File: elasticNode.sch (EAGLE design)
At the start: 101 parts, among them J1 ISP_CONN_6PIN, J2 FEMALE_HEADER_2X2, J3 FEMALE_HEADER_2X1, J4 FEMALE_HEADER_2X1, J5 FEMALE_HEADER_5X2, J6 FEMALE_HEADER_5X2, J7 JTAG_CONN_6PINTHT, J8 USB_CONN, U1 ATMEGA64AQFN, U10 LTC3419DFN, U2 SST26VF032B, U3 MRF24J40MA, U4 SPARTAN6-LX9, U5 SST26VF032B, U6 PAC1720, U7 PAC1720, U8 PAC1720, U9 FT232R, X1 12MHz, X2 50MHz, X3 32MHz

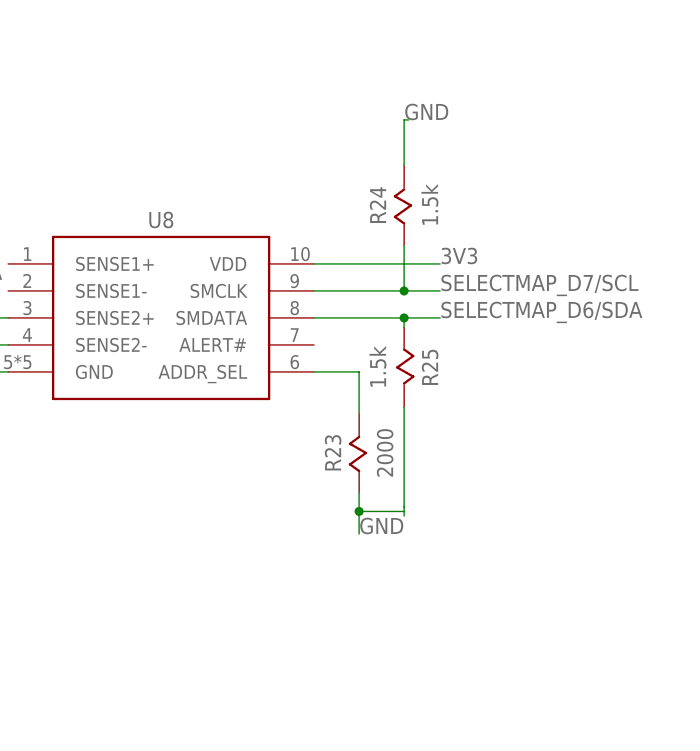
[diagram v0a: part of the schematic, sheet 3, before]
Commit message: changed i2c to pullup
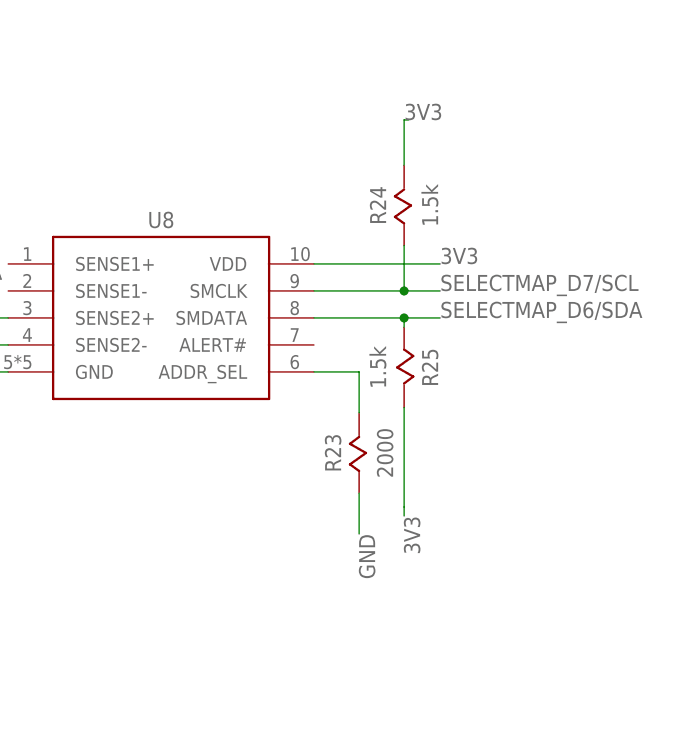
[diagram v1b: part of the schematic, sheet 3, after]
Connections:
- removed net N$33: R25.2
- net 3V3: now also R24.2, R25.2
- net GND: no longer R24.2
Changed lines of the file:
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@@
 <segment>
 <pinref part="R23" gate="G$1" pin="1"/>
-<wire x1="122" y1="-20.46" x2="122" y2="-22.5" width="0.1524" layer="91"/>
-<label x="122" y="-25" size="1.778" layer="95"/>
-<wire x1="122" y1="-22.5" x2="122" y2="-25" width="0.1524" layer="91"/>
-<wire x1="127" y1="-22.5" x2="122" y2="-22.5" width="0.1524" layer="91"/>
-<junction x="122" y="-22.5"/>
+<label x="122" y="-25" size="1.778" layer="95" rot="R270"/>
+<wire x1="122" y1="-20.46" x2="122" y2="-25" width="0.1524" layer="91"/>
 </segment>
 <segment>
@@
 <wire x1="70" y1="-7" x2="83" y2="-7" width="0.1524" layer="91"/>
 <label x="70" y="-7" size="1.778" layer="95" rot="R180"/>
-</segment>
-<segment>
-<pinref part="R24" gate="G$1" pin="2"/>
-<wire x1="127" y1="15.96" x2="127" y2="21" width="0.1524" layer="91"/>
-<wire x1="127" y1="21" x2="127.5" y2="21" width="0.1524" layer="91"/>
-<label x="127" y="21" size="1.778" layer="95"/>
 </segment>
 <segment>
@@
 <wire x1="-39" y1="8" x2="-39" y2="6.46" width="0.1524" layer="91"/>
 <label x="-27" y="0" size="1.778" layer="95"/>
+</segment>
+<segment>
+<pinref part="R24" gate="G$1" pin="2"/>
+<wire x1="127" y1="15.96" x2="127" y2="21" width="0.1524" layer="91"/>
+<wire x1="127" y1="21" x2="127.5" y2="21" width="0.1524" layer="91"/>
+<label x="127" y="21" size="1.778" layer="95"/>
+</segment>
+<segment>
+<pinref part="R25" gate="G$1" pin="2"/>
+<wire x1="127" y1="-10.96" x2="127" y2="-22" width="0.1524" layer="91"/>
+<wire x1="127" y1="-23" x2="127" y2="-22" width="0.1524" layer="91"/>
+<label x="127" y="-23" size="1.778" layer="95" rot="R270"/>
 </segment>
 </net>
@@
 </segment>
 </net>
-<net name="N$33" class="0">
-<segment>
-<pinref part="R25" gate="G$1" pin="2"/>
-<wire x1="127" y1="-10.96" x2="127" y2="-22" width="0.1524" layer="91"/>
-<wire x1="127" y1="-23" x2="127" y2="-22" width="0.1524" layer="91"/>
-</segment>
-</net>

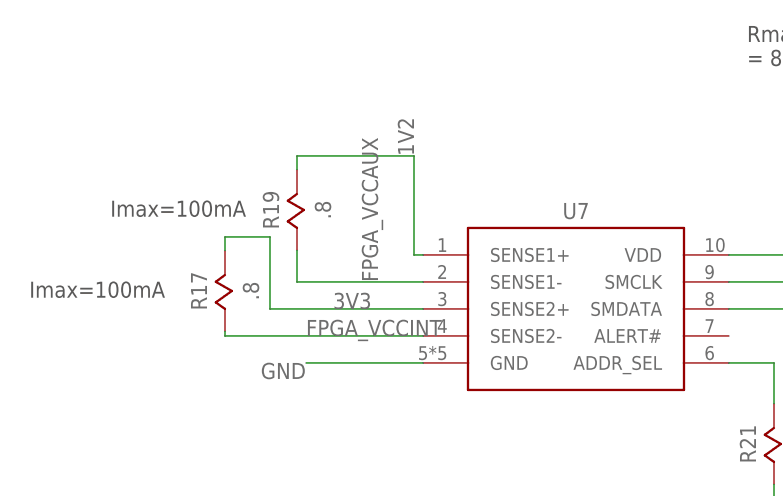
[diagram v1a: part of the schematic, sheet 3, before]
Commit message: updated board for previous pullups and swapped fpga power rails
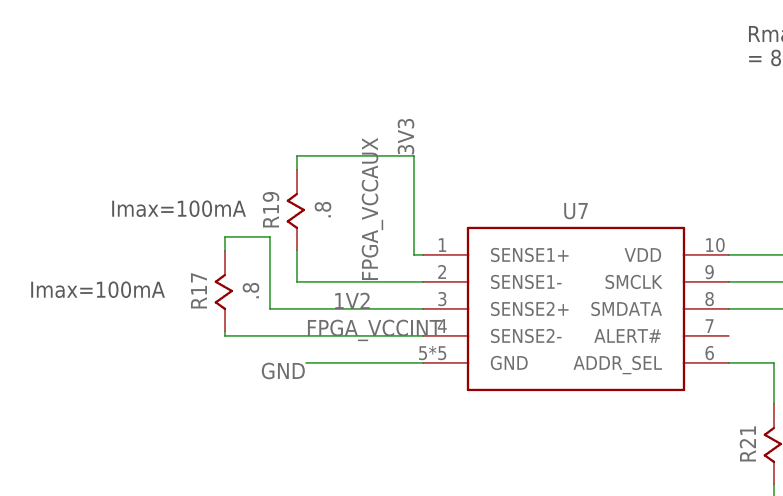
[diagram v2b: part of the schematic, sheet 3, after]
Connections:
- net 1V2: now also R17.2, U7.SENSE2+; no longer R19.2, U7.SENSE1+
- net 3V3: now also R19.2, U7.SENSE1+; no longer R17.2, U7.SENSE2+
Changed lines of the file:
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@@
-</segment>
-<segment>
-<pinref part="U7" gate="G$1" pin="SENSE2+"/>
-<wire x1="-17" y1="0" x2="-34" y2="0" width="0.1524" layer="91"/>
-<wire x1="-34" y1="0" x2="-34" y2="8" width="0.1524" layer="91"/>
-<wire x1="-34" y1="8" x2="-39" y2="8" width="0.1524" layer="91"/>
-<pinref part="R17" gate="G$1" pin="2"/>
-<wire x1="-39" y1="8" x2="-39" y2="6.46" width="0.1524" layer="91"/>
-<label x="-27" y="0" size="1.778" layer="95"/>
 </segment>
 <segment>
@@
 <wire x1="127" y1="-23" x2="127" y2="-22" width="0.1524" layer="91"/>
 <label x="127" y="-23" size="1.778" layer="95" rot="R270"/>
+</segment>
+<segment>
+<pinref part="U7" gate="G$1" pin="SENSE1+"/>
+<wire x1="-17" y1="6" x2="-18" y2="6" width="0.1524" layer="91"/>
+<wire x1="-18" y1="6" x2="-18" y2="17" width="0.1524" layer="91"/>
+<wire x1="-18" y1="17" x2="-31" y2="17" width="0.1524" layer="91"/>
+<pinref part="R19" gate="G$1" pin="2"/>
+<wire x1="-31" y1="17" x2="-31" y2="15.46" width="0.1524" layer="91"/>
+<label x="-18" y="17" size="1.778" layer="95" rot="R90"/>
 </segment>
 </net>
@@
 <net name="1V2" class="1">
 <segment>
-<pinref part="U7" gate="G$1" pin="SENSE1+"/>
-<wire x1="-17" y1="6" x2="-18" y2="6" width="0.1524" layer="91"/>
-<wire x1="-18" y1="6" x2="-18" y2="17" width="0.1524" layer="91"/>
-<wire x1="-18" y1="17" x2="-31" y2="17" width="0.1524" layer="91"/>
-<pinref part="R19" gate="G$1" pin="2"/>
-<wire x1="-31" y1="17" x2="-31" y2="15.46" width="0.1524" layer="91"/>
-<label x="-18" y="17" size="1.778" layer="95" rot="R90"/>
+<pinref part="U7" gate="G$1" pin="SENSE2+"/>
+<wire x1="-17" y1="0" x2="-34" y2="0" width="0.1524" layer="91"/>
+<wire x1="-34" y1="0" x2="-34" y2="8" width="0.1524" layer="91"/>
+<wire x1="-34" y1="8" x2="-39" y2="8" width="0.1524" layer="91"/>
+<pinref part="R17" gate="G$1" pin="2"/>
+<wire x1="-39" y1="8" x2="-39" y2="6.46" width="0.1524" layer="91"/>
+<label x="-27" y="0" size="1.778" layer="95"/>
 </segment>
 </net>

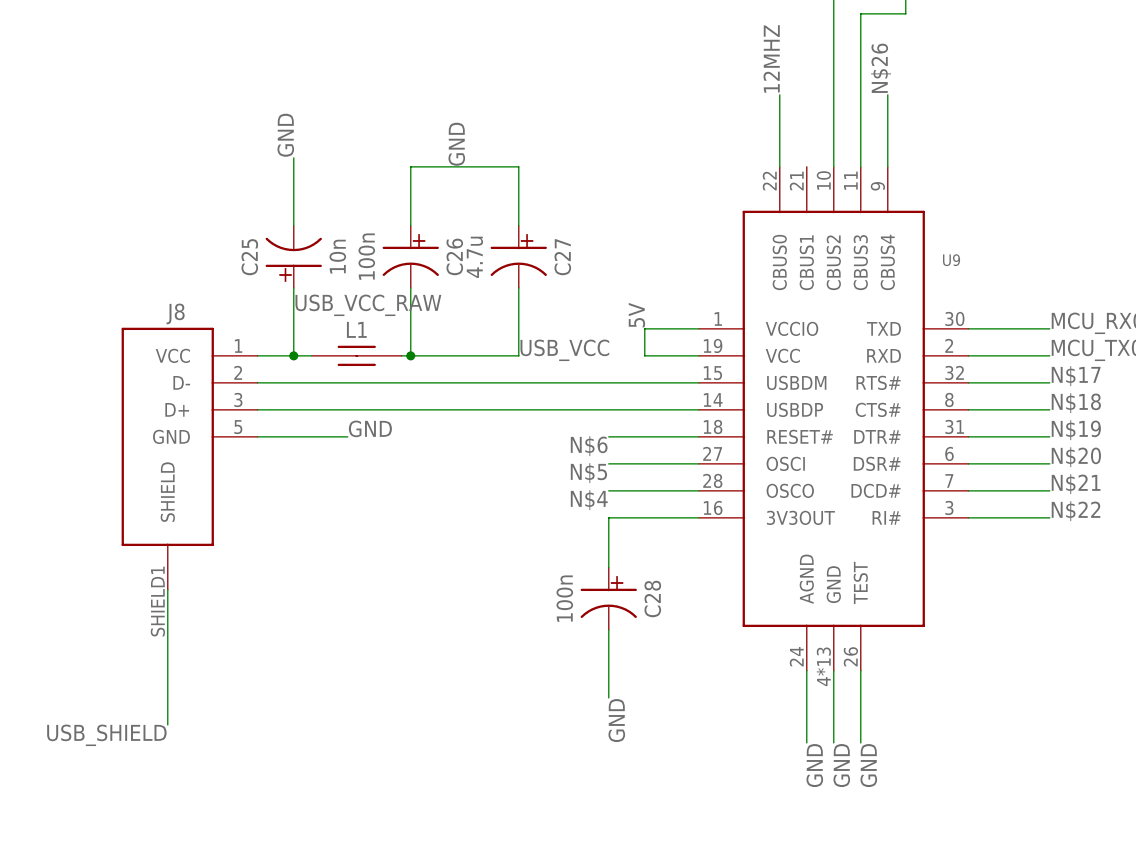
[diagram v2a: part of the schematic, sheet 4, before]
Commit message: added smd usb connector
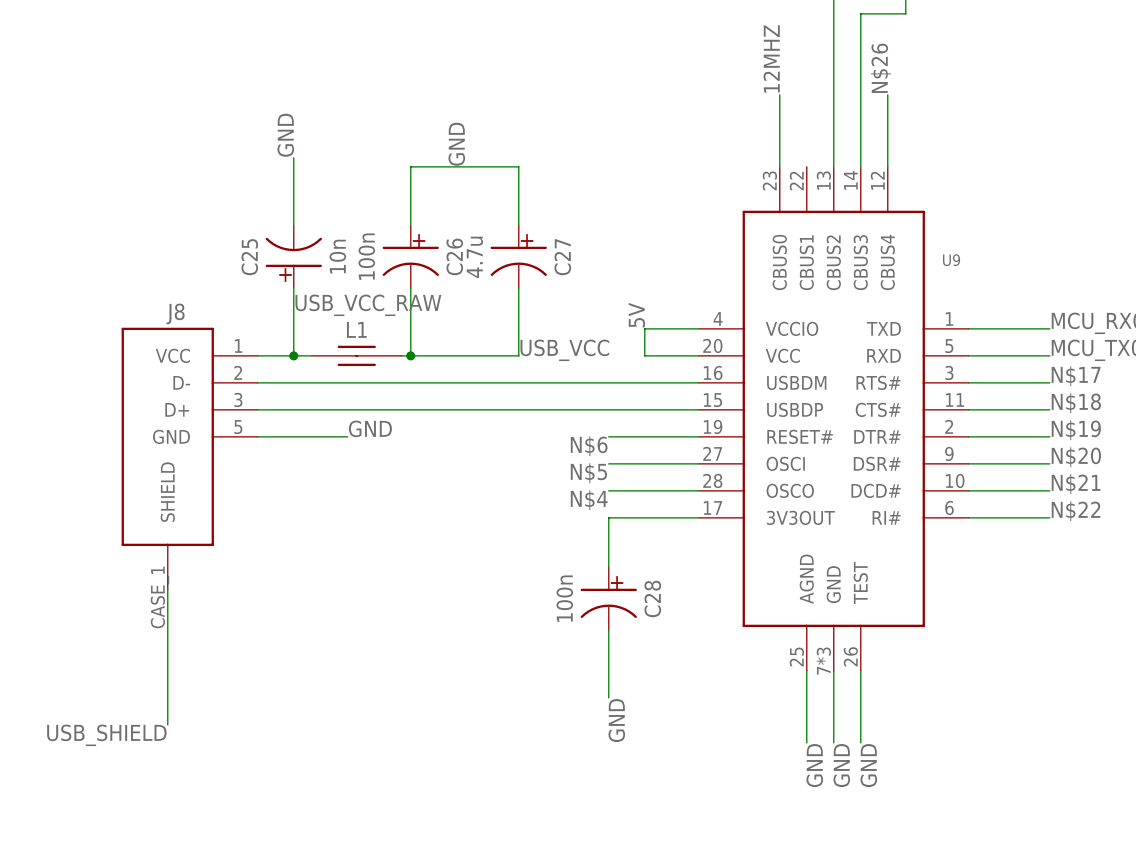
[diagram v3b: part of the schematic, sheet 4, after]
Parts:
- J8: value USB_CONN -> USB_CONNSMT; device connectors:USB_CONN -> connectors:USB_CONNSMT
- U9: value FT232R -> FT232RSSOP28; device ic:FT232R -> ic:FT232RSSOP28
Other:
- moved on the sheet: J8, U9
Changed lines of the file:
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@@
 <part name="L2" library="passive" deviceset="INDUCTOR" device="" value="3.3uH"/>
 <part name="U3" library="wireless" deviceset="MRF24J40MA" device=""/>
-<part name="U9" library="ic" deviceset="FT232R" device=""/>
-<part name="J8" library="connectors" deviceset="USB_CONN" device=""/>
+<part name="U9" library="ic" deviceset="FT232R" device="SSOP28"/>
+<part name="J8" library="connectors" deviceset="USB_CONN" device="SMT"/>
 <part name="L1" library="passive" deviceset="FERRITE_BEAD" device="" value="40Ohm 1.5A"/>
 <part name="C28" library="passive" deviceset="CAPACITOR" device="0805" value="100n"/>

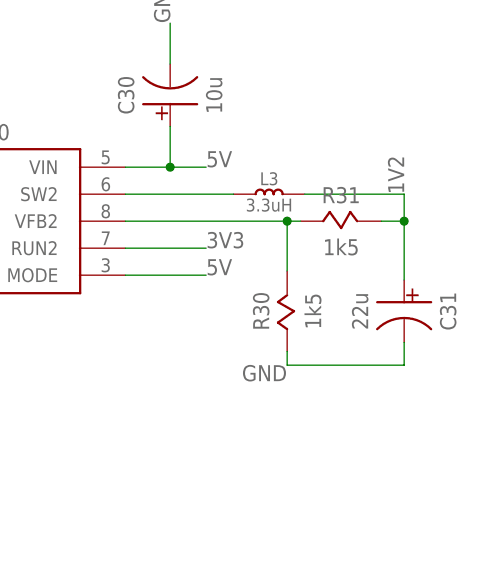
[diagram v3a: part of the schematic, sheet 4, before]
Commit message: updated footprints, moved reset buttons, general reorganising
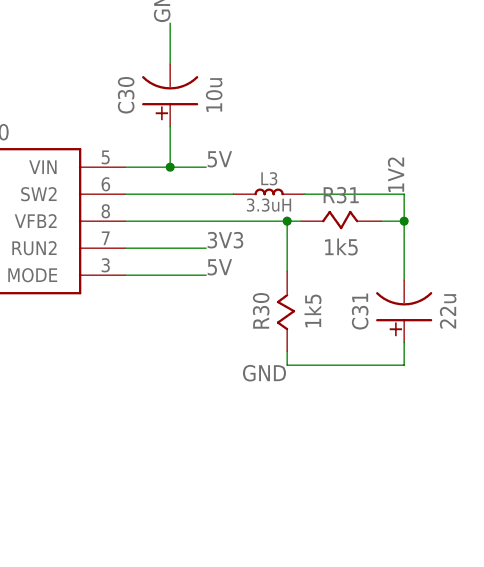
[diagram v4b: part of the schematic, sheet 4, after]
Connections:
- net N$38 renamed XTAL2
- net N$39 renamed XTAL1
- removed net MCU_CS: U1.PB0_SS#
- net 1V2: now also C31.P$2; no longer C31.P$1
- net FPGA_RESET: now also U1.PB6_OC1B
- net GND: now also C31.P$1; no longer C31.P$2
- net MCU_LED0: now also U1.PB5_OC1A; no longer U1.PB6_OC1B
- net MCU_LED1: now also U1.PB0_SS#; no longer U1.PB5_OC1A
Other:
- moved on the sheet: C31
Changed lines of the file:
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@@
 <?xml version="1.0" encoding="utf-8"?>
 <!DOCTYPE eagle SYSTEM "eagle.dtd">
-<eagle version="8.2.2">
+<eagle version="8.2.0">
 <drawing>
 <settings>
@@
 </segment>
 </net>
-<net name="MCU_CS" class="0">
-<segment>
-<pinref part="U1" gate="G$1" pin="PB0_SS#"/>
-<wire x1="-42" y1="-1" x2="-54" y2="-1" width="0.1524" layer="91"/>
-<label x="-54" y="-1" size="1.778" layer="95" rot="R180"/>
-</segment>
-</net>
 <net name="A8" class="0">
 <segment>
@@
 </segment>
 <segment>
-<pinref part="U1" gate="G$1" pin="PB6_OC1B"/>
-<wire x1="-54" y1="-19" x2="-42" y2="-19" width="0.1524" layer="91"/>
-<label x="-54" y="-19" size="1.778" layer="95" rot="R180"/>
+<pinref part="U1" gate="G$1" pin="PB5_OC1A"/>
+<wire x1="-42" y1="-16" x2="-54" y2="-16" width="0.1524" layer="91"/>
+<label x="-54" y="-16" size="1.778" layer="95" rot="R180"/>
 </segment>
 </net>
@@
 </segment>
 <segment>
-<pinref part="U1" gate="G$1" pin="PB5_OC1A"/>
-<wire x1="-42" y1="-16" x2="-54" y2="-16" width="0.1524" layer="91"/>
-<label x="-54" y="-16" size="1.778" layer="95" rot="R180"/>
+<pinref part="U1" gate="G$1" pin="PB0_SS#"/>
+<wire x1="-42" y1="-1" x2="-54" y2="-1" width="0.1524" layer="91"/>
+<label x="-54" y="-1" size="1.778" layer="95" rot="R180"/>
 </segment>
 </net>
@@
 </segment>
 </net>
-<net name="N$38" class="0">
+<net name="XTAL2" class="0">
 <segment>
 <pinref part="X1" gate="G$1" pin="P$1"/>
@@
 </segment>
 </net>
-<net name="N$39" class="0">
+<net name="XTAL1" class="0">
 <segment>
 <pinref part="U1" gate="G$1" pin="XTAL1"/>
@@
 <pinref part="X1" gate="G$1" pin="P$2"/>
 <wire x1="68" y1="17" x2="68" y2="14" width="0.1524" layer="91"/>
+</segment>
+</net>
+<net name="FPGA_RESET" class="0">
+<segment>
+<pinref part="U1" gate="G$1" pin="PB6_OC1B"/>
+<wire x1="-54" y1="-19" x2="-42" y2="-19" width="0.1524" layer="91"/>
+<label x="-54" y="-19" size="1.778" layer="95" rot="R180"/>
 </segment>
 </net>
@@
 <instance part="R30" gate="G$1" x="34" y="-12" rot="R90"/>
 <instance part="R29" gate="G$1" x="-29" y="-12" rot="R270"/>
-<instance part="C31" gate="G$1" x="47" y="-12" rot="R270"/>
+<instance part="C31" gate="G$1" x="47" y="-12" rot="R90"/>
 <instance part="C29" gate="G$1" x="-41" y="-12" rot="R270"/>
 <instance part="C30" gate="G$1" x="21" y="12" rot="R90"/>
@@
 </segment>
 <segment>
-<pinref part="C31" gate="G$1" pin="P$2"/>
-<wire x1="47" y1="-15.46" x2="47" y2="-18" width="0.1524" layer="91"/>
 <pinref part="R30" gate="G$1" pin="1"/>
 <wire x1="47" y1="-18" x2="34" y2="-18" width="0.1524" layer="91"/>
 <wire x1="34" y1="-18" x2="34" y2="-16.46" width="0.1524" layer="91"/>
 <label x="34" y="-18" size="1.778" layer="95" rot="R180"/>
+<pinref part="C31" gate="G$1" pin="P$1"/>
+<wire x1="47" y1="-15.46" x2="47" y2="-18" width="0.1524" layer="91"/>
 </segment>
 <segment>
@@
 <segment>
 <pinref part="R31" gate="G$1" pin="2"/>
-<pinref part="C31" gate="G$1" pin="P$1"/>
 <wire x1="44.46" y1="-2" x2="47" y2="-2" width="0.1524" layer="91"/>
-<wire x1="47" y1="-2" x2="47" y2="-8.54" width="0.1524" layer="91"/>
 <label x="47" y="1" size="1.778" layer="95" rot="R90"/>
 <pinref part="L3" gate="G$1" pin="P$2"/>
 <wire x1="35.96" y1="1" x2="47" y2="1" width="0.1524" layer="91"/>
 <wire x1="47" y1="1" x2="47" y2="-2" width="0.1524" layer="91"/>
+<pinref part="C31" gate="G$1" pin="P$2"/>
+<wire x1="47" y1="-8.54" x2="47" y2="-2" width="0.1524" layer="91"/>
 <junction x="47" y="-2"/>
 </segment>
